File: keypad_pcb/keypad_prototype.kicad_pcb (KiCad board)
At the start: 2 copper layers, 40 x 60 mm, 31 parts

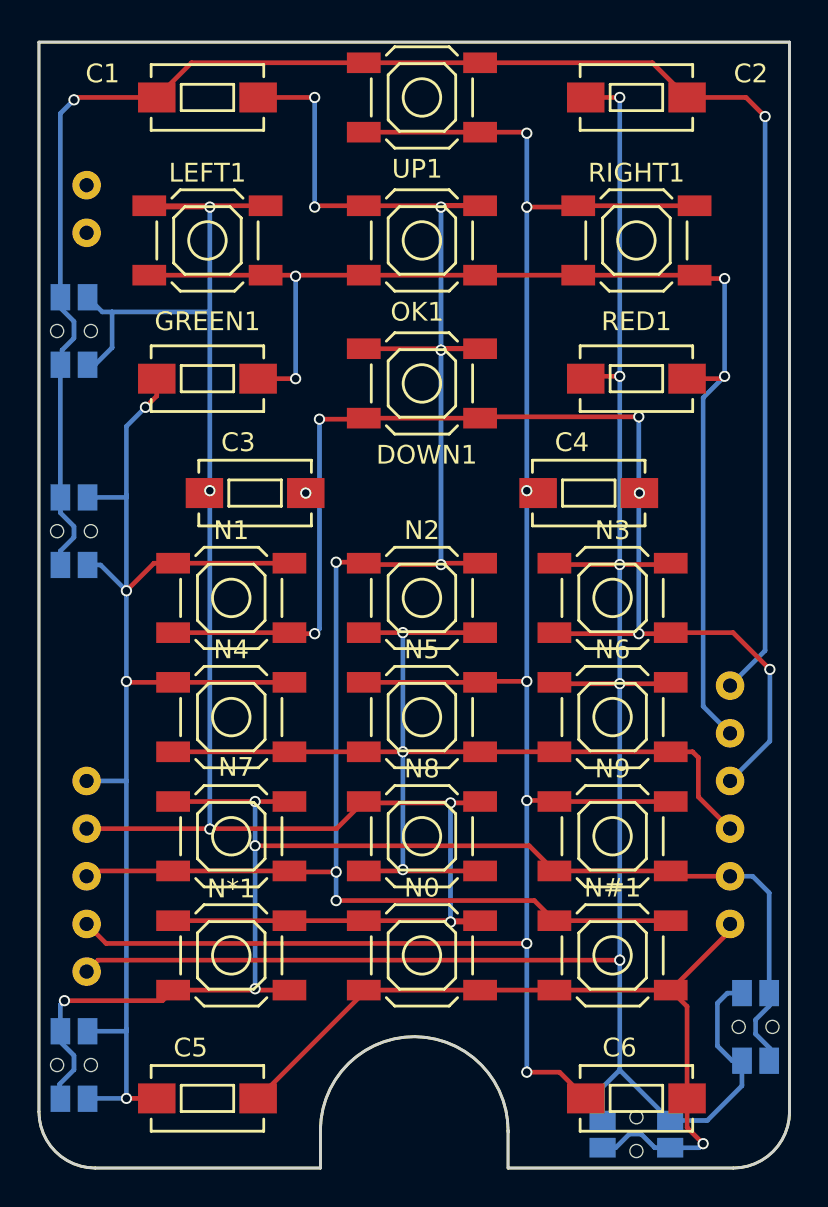
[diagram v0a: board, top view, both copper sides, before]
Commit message: New keypad PCB
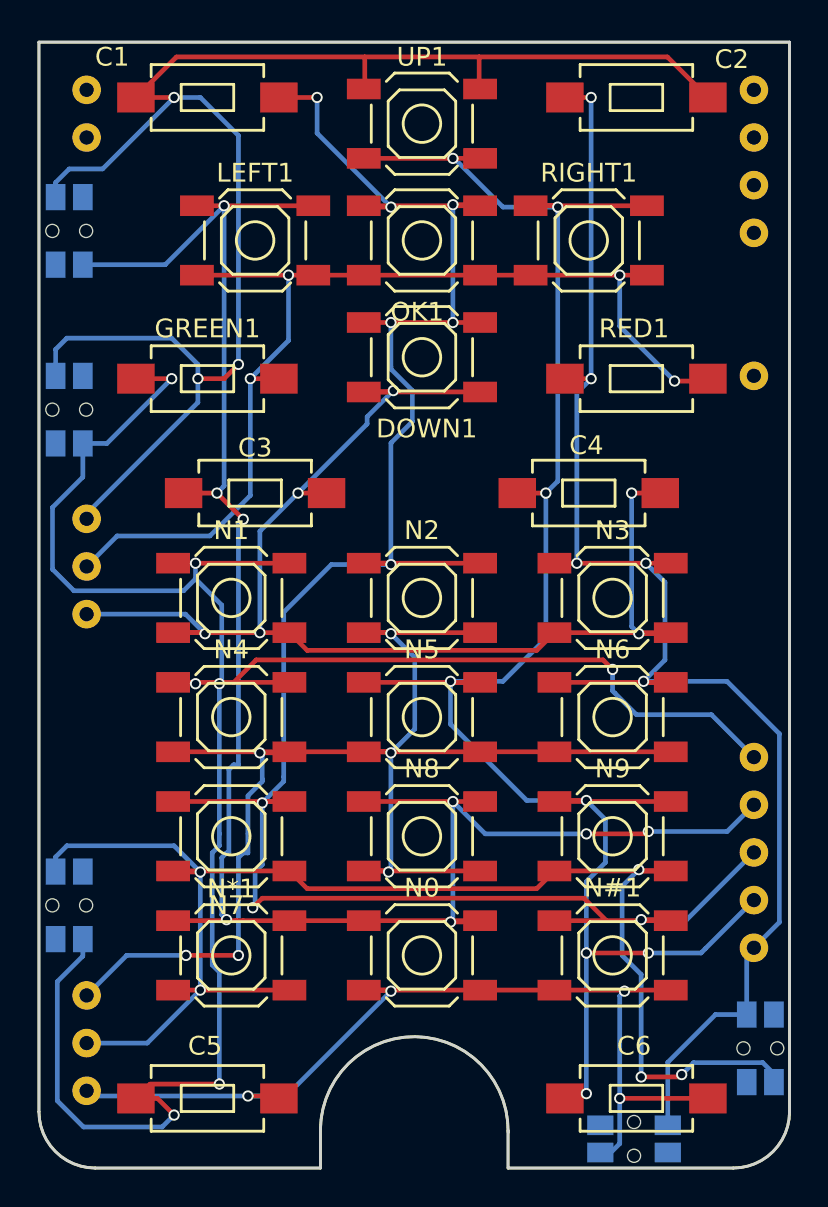
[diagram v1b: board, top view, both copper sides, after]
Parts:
- ?: footprint keypad_overlay:KEYPAD_OVERLAY -> common_footprints:keypad_overlay
- C1, C2, C3, C4, C5, C6, GREEN1, RED1: value (none) -> AB2_SWITCH_MOMENTARY; footprint Buttons_Switches_SMD:SW_SPST_EVQPE1 -> footprints:SW_SPST_EVQPE1
- DOWN1, LEFT1, N#1, N*1, N0, N1, N2, N3, N4, N5, N6, N7, N8, N9, OK1, RIGHT1, UP1: value (none) -> AB2_SWITCH_MOMENTARY
- OPTION1, PHOTO1, PHOTO2, VOL_DOWN1, VOL_UP1: value (none) -> AB2_SWITCH_MOMENTARY; footprint Buttons_Switches_SMD:SW_SPST_EVQP7C -> footprints:SW_SPST_EVQP7C
- moved OPTION1 8.51 mm to (150.1, 151.0)
- moved VOL_DOWN1 6.48 mm to (150.1, 124.6)
- moved VOL_UP1 5.34 mm to (150.1, 115.1)
- moved LEFT1 2.54 mm to (160.0, 115.6)
- moved RIGHT1 2.54 mm to (177.8, 115.6)
- moved DOWN1 1.40 mm to (168.9, 121.8)
- moved UP1 1.40 mm to (168.9, 109.3)
- moved PHOTO1 1.17 mm to (186.9, 158.6)
- moved PHOTO2 0.28 mm to (180.2, 163.4)
- turned N7 to 0 degrees
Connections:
- ? pad 12: Net-(U1-Pad12) -> (no net)
- ? pad 13: Net-(U1-Pad13) -> (no net)
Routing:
- net Net-(C5-Pad1): track 69.9 -> 120.8 mm, vias 4 -> 7
- net Net-(C2-Pad1): track 114.9 -> 81.7 mm
- net Net-(N2-Pad2): track 57.9 -> 79.1 mm, vias 3 -> 6
- net Net-(C1-Pad1): track 104.7 -> 118.4 mm, vias 8 -> 9
- net Net-(C1-Pad2): track 96.2 -> 86.2 mm, vias 2 -> 3
- net Net-(GREEN1-Pad2): track 65.7 -> 57.1 mm
- net Net-(C5-Pad2): track 44.2 -> 52.5 mm, vias 1 -> 4
- net Net-(N*1-Pad2): track 72.6 -> 79.5 mm, vias 4 -> 5
- net Net-(C4-Pad1): track 112.4 -> 106.1 mm, vias 7 -> 8
- net Net-(C3-Pad1): track 99.4 -> 104.6 mm, vias 5 -> 8
- net Net-(C3-Pad2): track 67.7 -> 72.1 mm, vias 7 -> 6
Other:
- board text added: "Sorry, this side is not symmetric. The front side is much prettier, go look at it instead!"

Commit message: Rerouted one track that wasn't beautiful
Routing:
- net Net-(C1-Pad1): track 118.4 -> 121.8 mm
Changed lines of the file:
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@@
     (thickness 1.6)
     (drawings 12)
-    (tracks 403)
+    (tracks 405)
     (zones 0)
     (modules 31)
@@
   (gr_line (start 173.5 165) (end 185.5 165) (angle 90) (layer Edge.Cuts) (width 0.15))
   (gr_line (start 151.5 165) (end 163.5 165) (angle 90) (layer Edge.Cuts) (width 0.15))
+  (segment (start 159 108) (end 161.24 108) (width 0.25) (layer F.Cu) (net 1))
+  (segment (start 161.24 108) (end 161.29 107.95) (width 0.25) (layer F.Cu) (net 1))
+  (segment (start 160.855 109.855) (end 159 108) (width 0.25) (layer B.Cu) (net 1))
+  (via (at 159 108) (size 0.6) (drill 0.4) (layers F.Cu B.Cu) (net 1))
+  (segment (start 163.322 109.855) (end 160.855 109.855) (width 0.25) (layer B.Cu) (net 1))
   (segment (start 167.259 122.301) (end 167.259 122.428) (width 0.25) (layer B.Cu) (net 1))
   (segment (start 168.402 125.222) (end 167.259 126.365) (width 0.25) (layer B.Cu) (net 1))
@@
   (segment (start 167.259 132.842) (end 167.259 126.365) (width 0.25) (layer B.Cu) (net 1))
   (segment (start 167.259 122.301) (end 167.259 119.943) (width 0.25) (layer B.Cu) (net 1))
-  (segment (start 161.29 107.95) (end 163.322 107.95) (width 0.25) (layer F.Cu) (net 1))
   (segment (start 167.259 113.792) (end 165.882 113.792) (width 0.25) (layer F.Cu) (net 1))
   (via (at 167.259 113.792) (size 0.6) (drill 0.4) (layers F.Cu B.Cu) (net 1))
   (segment (start 163.322 109.855) (end 167.259 113.792) (width 0.25) (layer B.Cu) (net 1))
-  (segment (start 163.322 107.95) (end 163.322 109.855) (width 0.25) (layer B.Cu) (net 1))
-  (via (at 163.322 107.95) (size 0.6) (drill 0.4) (layers F.Cu B.Cu) (net 1))
   (segment (start 165.882 113.792) (end 165.81 113.72) (width 0.25) (layer F.Cu) (net 1))
   (segment (start 182.17 151.82) (end 178.744 151.82) (width 0.25) (layer F.Cu) (net 1))
@@
   (segment (start 158.369 122.936) (end 159.131 122.174) (width 0.25) (layer F.Cu) (net 2))
   (segment (start 158.369 122.936) (end 156.972 122.936) (width 0.25) (layer F.Cu) (net 2))
-  (segment (start 151.0411 130.4036) (end 151.0411 130.1369) (width 0.25) (layer B.Cu) (net 2) (status C00000))
-  (segment (start 151.0411 130.1369) (end 156.972 124.206) (width 0.25) (layer B.Cu) (net 2) (status 400000))
+  (segment (start 151.0411 130.4036) (end 151.0411 130.1369) (width 0.25) (layer B.Cu) (net 2))
+  (segment (start 151.0411 130.1369) (end 156.972 124.206) (width 0.25) (layer B.Cu) (net 2))
   (segment (start 156.972 124.206) (end 156.972 122.936) (width 0.25) (layer B.Cu) (net 2))
   (segment (start 156.972 122.936) (end 156.972 122.174) (width 0.25) (layer B.Cu) (net 2))
-  (segment (start 149.389 121.375) (end 149.389 122.787) (width 0.25) (layer B.Cu) (net 2) (status 800000))
+  (segment (start 149.389 121.375) (end 149.389 122.787) (width 0.25) (layer B.Cu) (net 2))
   (segment (start 149.987 120.777) (end 149.389 121.375) (width 0.25) (layer B.Cu) (net 2))
   (segment (start 155.575 120.777) (end 149.987 120.777) (width 0.25) (layer B.Cu) (net 2))
@@
   (segment (start 177.165 132.77) (end 180.848 132.77) (width 0.25) (layer F.Cu) (net 3))
   (segment (start 180.848 132.77) (end 182.17 132.77) (width 0.25) (layer F.Cu) (net 3))
-  (segment (start 150.839 116.862) (end 155.227 116.862) (width 0.25) (layer B.Cu) (net 4) (status 400000))
+  (segment (start 150.839 116.862) (end 155.227 116.862) (width 0.25) (layer B.Cu) (net 4))
   (segment (start 155.227 116.862) (end 158.369 113.72) (width 0.25) (layer B.Cu) (net 4))
   (segment (start 155.65 151.82) (end 158.496 151.82) (width 0.25) (layer F.Cu) (net 4))
@@
   (segment (start 165.989 125.349) (end 165.989 124.968) (width 0.25) (layer B.Cu) (net 5))
   (segment (start 162.306 129.032) (end 165.989 125.349) (width 0.25) (layer B.Cu) (net 5))
-  (segment (start 167.314 123.643) (end 165.81 123.643) (width 0.25) (layer F.Cu) (net 5) (status 800000))
+  (segment (start 167.314 123.643) (end 165.81 123.643) (width 0.25) (layer F.Cu) (net 5))
   (segment (start 167.386 123.571) (end 167.314 123.643) (width 0.25) (layer F.Cu) (net 5))
   (via (at 167.386 123.571) (size 0.6) (drill 0.4) (layers F.Cu B.Cu) (net 5))
@@
   (segment (start 165.81 111.197) (end 170.561 111.197) (width 0.25) (layer F.Cu) (net 6))
   (segment (start 170.561 111.197) (end 172.01 111.197) (width 0.25) (layer F.Cu) (net 6))
-  (segment (start 150.839 126.387) (end 152.124 126.387) (width 0.25) (layer B.Cu) (net 7) (status 400000))
-  (segment (start 155.575 122.936) (end 153.67 122.936) (width 0.25) (layer F.Cu) (net 7) (status 800000))
+  (segment (start 150.839 126.387) (end 152.124 126.387) (width 0.25) (layer B.Cu) (net 7))
+  (segment (start 155.575 122.936) (end 153.67 122.936) (width 0.25) (layer F.Cu) (net 7))
   (via (at 155.575 122.936) (size 0.6) (drill 0.4) (layers F.Cu B.Cu) (net 7))
   (segment (start 152.124 126.387) (end 155.575 122.936) (width 0.25) (layer B.Cu) (net 7))

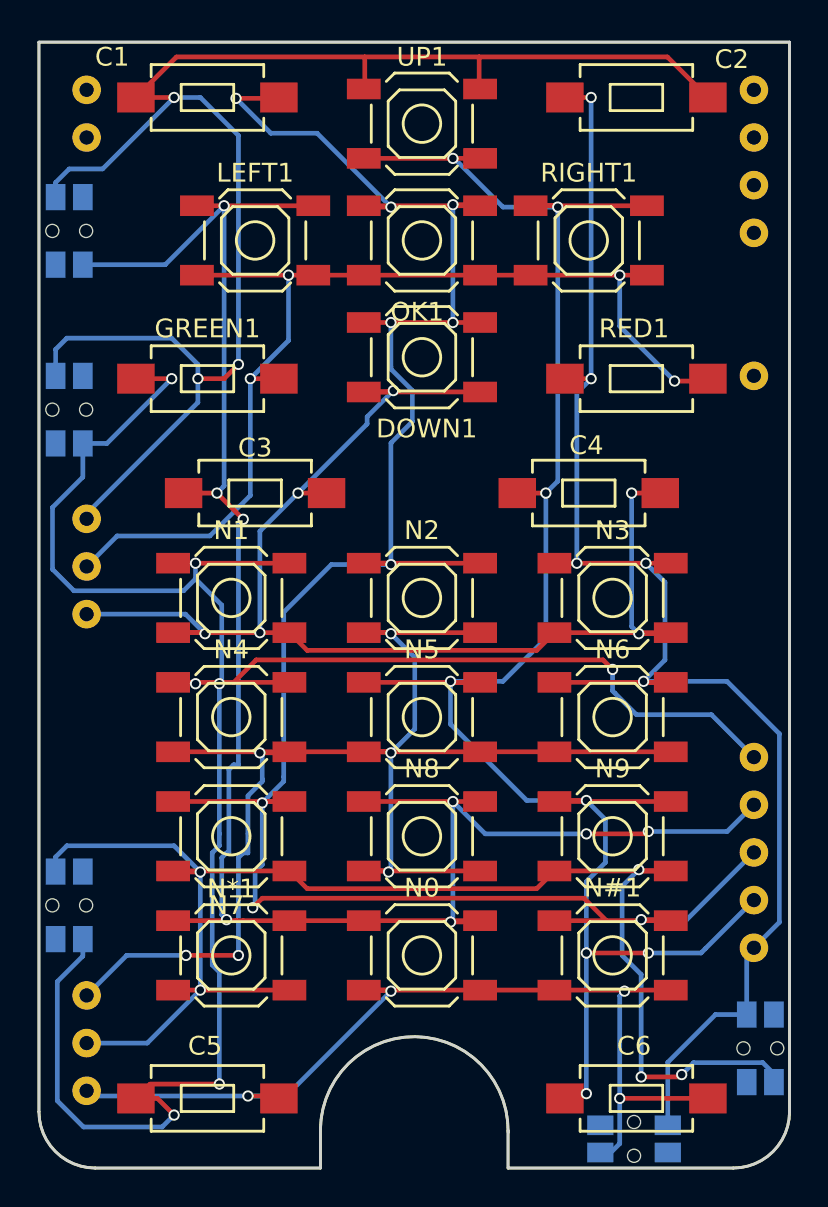
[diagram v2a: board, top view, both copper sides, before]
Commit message: Added hacker glider symbol and version info to keypad board; regenerated gerbers
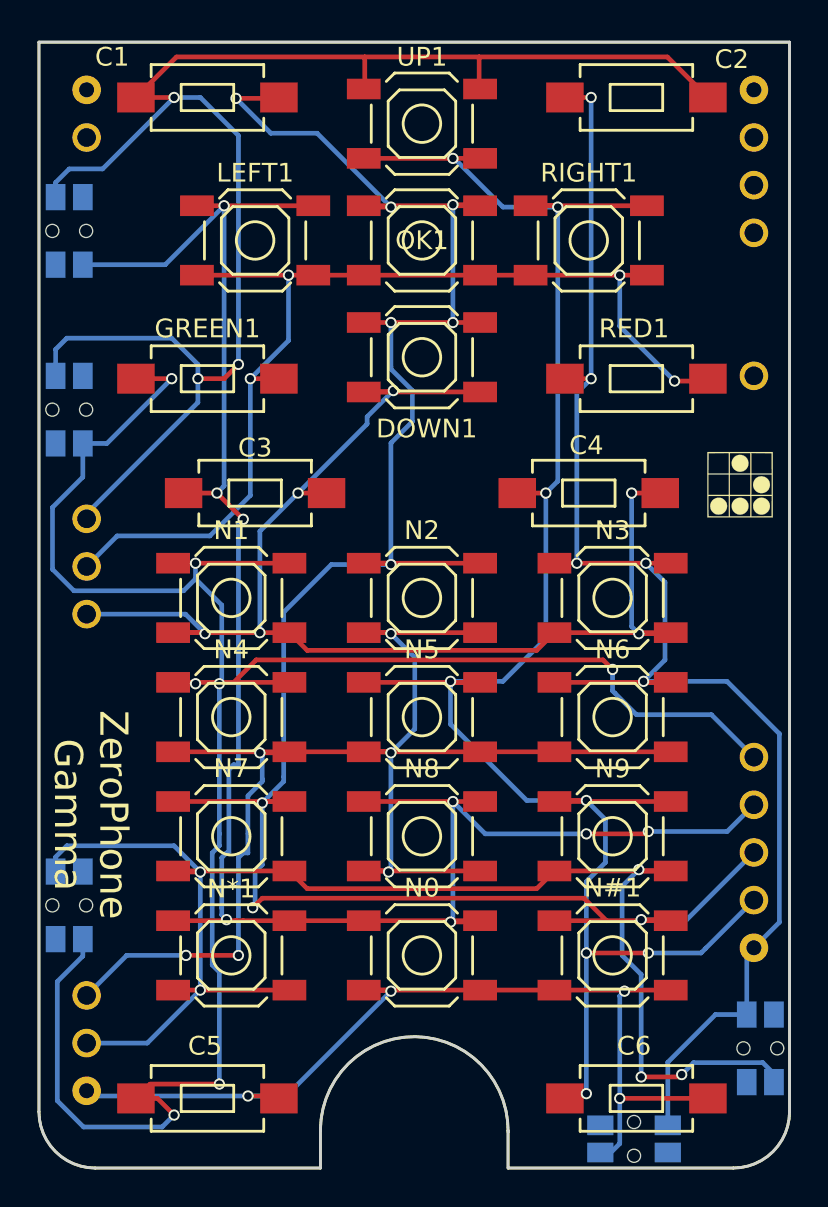
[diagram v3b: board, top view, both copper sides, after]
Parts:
- added G***: LOGO, art:glider, F.Cu at (185.9, 128.6)
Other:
- board text added: "ZeroPhone Gamma"
